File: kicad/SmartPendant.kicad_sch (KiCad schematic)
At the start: 51 parts, among them J1 UART, J2 ST-LINK, J3 Conn_01x05, J4 TYPE-C16PIN, J5 Display, Q1 MMBT3904, U1 WEACT BLACKPILL F4X1, U2 AMS1117-3.3, U3 MB85RC256VPNF

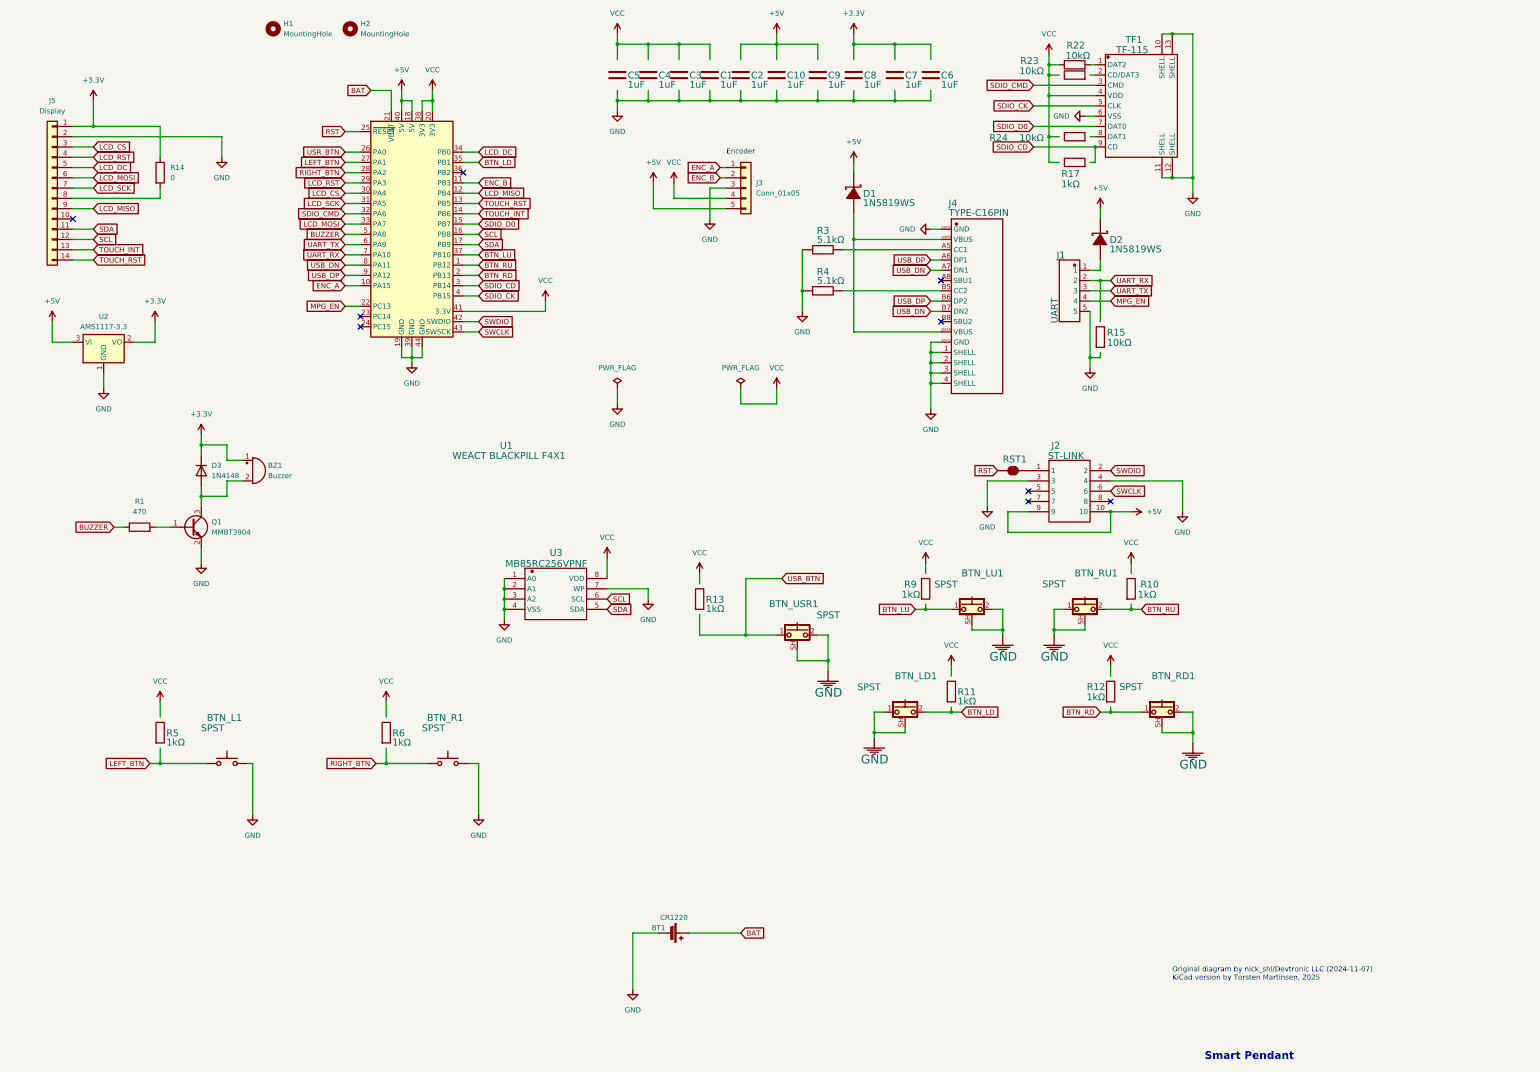
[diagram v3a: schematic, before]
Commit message: Fix ERC violations.
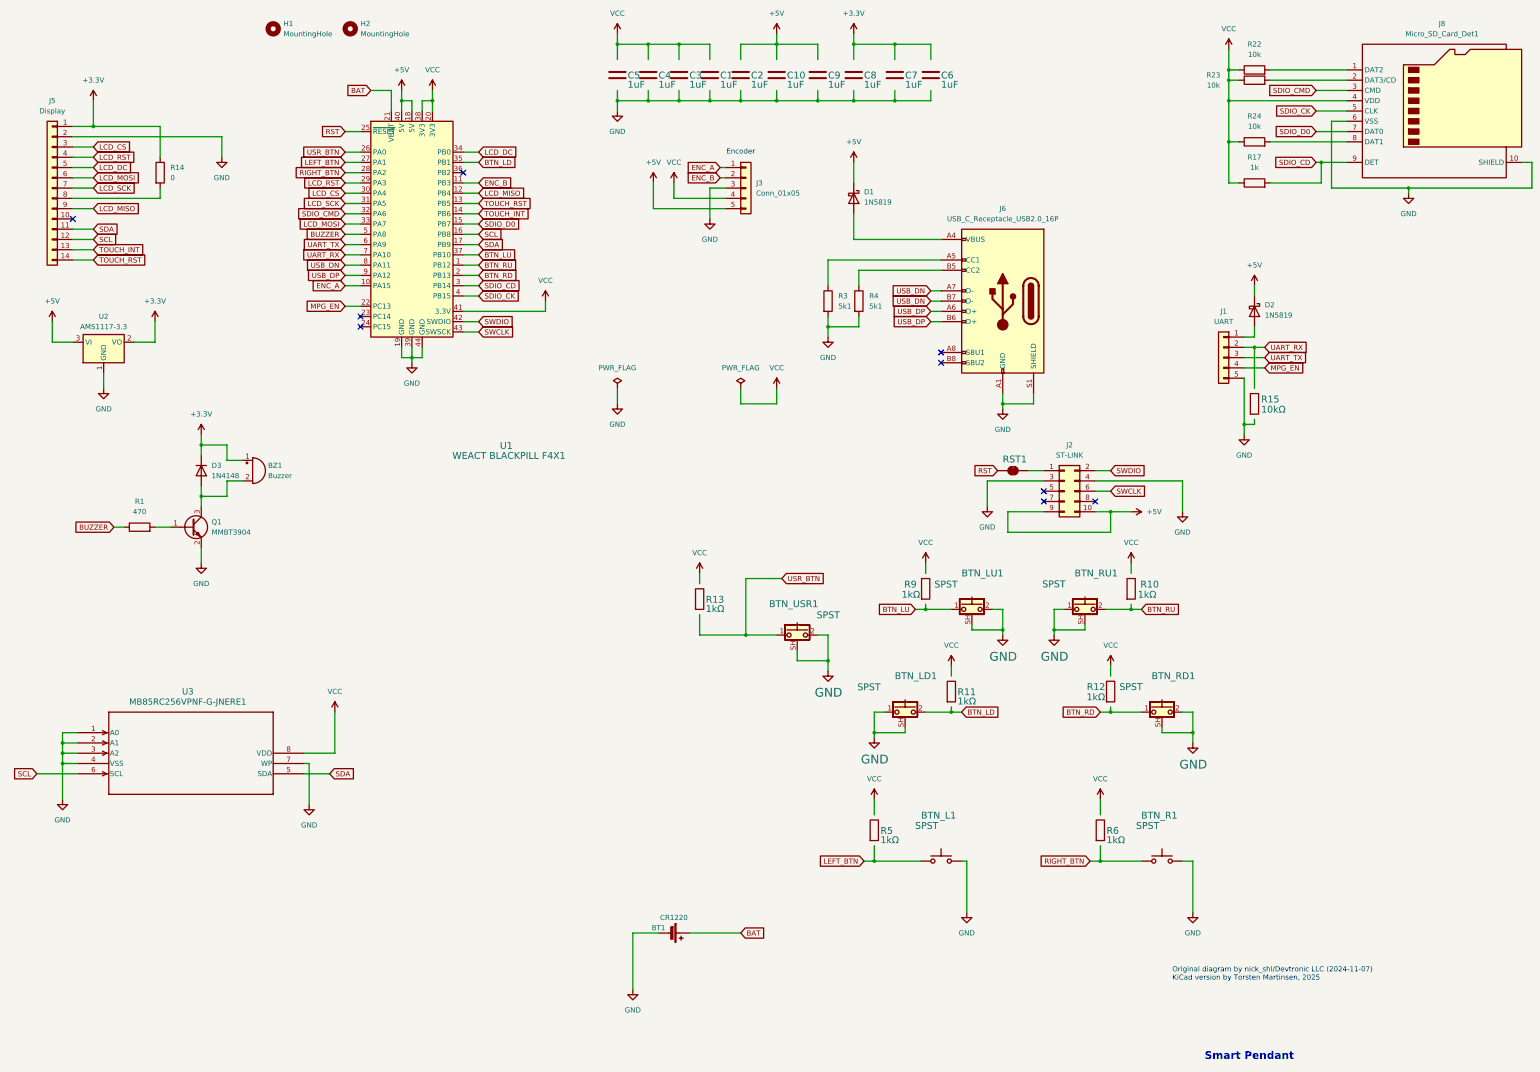
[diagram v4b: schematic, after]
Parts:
- removed D1: 1N5819WS, PCM_Diode_SMD_AKL:D_MiniMELF, symbol B5819WS_C22624
- removed D2: 1N5819WS, PCM_Diode_SMD_AKL:D_MiniMELF, symbol B5819WS_C22624_1
- removed J1: UART, Connector_JST:JST_XH_B5B-XH-A_1x05_P2.50mm_Vertical, symbol KF128-2.54-5P
- removed J2: ST-LINK, Connector_IDC:IDC-Header_2x05_P2.54mm_Horizontal, symbol 300R-10P
- removed J4: TYPE-C16PIN, Custom:USB_C_Receptacle_AliExpress_16pin, symbol TYPE-C16PIN
- removed R17: 1kΩ, PCM_Resistor_SMD_AKL:R_0603_1608Metric, symbol Device:R
- removed R23, R24: 10kΩ, PCM_Resistor_SMD_AKL:R_0603_1608Metric, symbol Device:R
- removed R3: 5.1kΩ, PCM_Resistor_SMD_AKL:R_0603_1608Metric, symbol 0805W8F1002T5E_8
- removed R4: 5.1kΩ, PCM_Resistor_SMD_AKL:R_0603_1608Metric, symbol 0805W8F1002T5E_9
- removed TF1: TF-115, Custom:J_SD_Card-micro_socket_A, symbol TF-115
- removed U3: MB85RC256VPNF, PCM_Package_SO_AKL:SOP-8_3.9x4.9mm_P1.27mm, symbol MB85RC256VPNF
- added D1, D2: 1N5819, PCM_Diode_SMD_AKL:D_SOD-123, symbol Device:D_Schottky
- added J1: UART, Connector_JST:JST_XH_B5B-XH-A_1x05_P2.50mm_Vertical, symbol Connector_Generic:Conn_01x05
- added J2: ST-LINK, Connector_IDC:IDC-Header_2x05_P2.54mm_Horizontal, symbol Connector_Generic:Conn_02x05_Odd_Even
- added J6: USB_C_Receptacle_USB2.0_16P, Custom:USB_C_Receptacle_AliExpress_16pin, symbol Connector:USB_C_Receptacle_USB2.0_16P
- added J8: Micro_SD_Card_Det1, Custom:J_SD_Card-micro_socket_A, symbol Connector:Micro_SD_Card_Det1
- added R17: 1k, PCM_Resistor_SMD_AKL:R_0603_1608Metric, symbol Device:R
- added R23, R24: 10k, PCM_Resistor_SMD_AKL:R_0603_1608Metric, symbol Device:R
- added R3, R4: 5k1, PCM_Resistor_SMD_AKL:R_0603_1608Metric, symbol Device:R
- added U3: MB85RC256VPNF-G-JNERE1, FPT-8P-M02_FUJ, symbol MB85RC256VPNF:MB85RC256VPNF-G-JNERE1
- R22: value 10kΩ -> 10k; Manufacturer UNI-ROYAL(厚声) -> (none); Manufacturer Part 0805W8F1002T5E -> (none); Supplier LCSC -> (none); Supplier Part C17414 -> (none)
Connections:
- net +5V: now also D1.1 (K), D2.1 (K), J2.10 (Pin_10), J2.9 (Pin_9)
- net GND: now also J1.5 (Pin_5), J2.3 (Pin_3), J2.4 (Pin_4), J6.A1 (GND), J6.A12 (GND), J6.B1 (GND), J6.B12 (GND), J6.S1 (SHIELD), J8.10 (SHIELD), J8.6 (VSS), R3.2, R4.2, U3.1 (A0), U3.2 (A1), U3.3 (A2), U3.4 (VSS), U3.7 (WP); no longer BTN_LD1.1, BTN_LD1.SH (B), BTN_LU1.2, BTN_LU1.SH (B), BTN_RD1.2, BTN_RD1.SH (B), BTN_RU1.1, BTN_RU1.SH (B), BTN_USR1.2, BTN_USR1.SH (B)
- net MPG_EN: now also J1.4 (Pin_4)
- net SCL: now also U3.6 (SCL)
- net SDA: now also U3.5 (SDA)
- net SDIO_CD: now also J8.9 (DET), R17.2
- net SDIO_CK: now also J8.5 (CLK)
- net SDIO_CMD: now also J8.3 (CMD)
- net SDIO_D0: now also J8.7 (DAT0)
- net SWCLK: now also J2.6 (Pin_6)
- net SWDIO: now also J2.2 (Pin_2)
- net UART_RX: now also J1.2 (Pin_2)
- net UART_TX: now also J1.3 (Pin_3)
- net USB_DN: now also J6.A7 (D-), J6.B7 (D-)
- net USB_DP: now also J6.A6 (D+), J6.B6 (D+)
- net VCC: now also J8.4 (VDD), R17.1, R23.1, R24.1, U3.8 (VDD)
- net at RST1.2 (B): now also J2.1 (Pin_1)
- net at R22.2: now also J8.1 (DAT2)
- new net: D2.2 (A), J1.1 (Pin_1)
- new net: BTN_LU1.2, BTN_LU1.SH (B)
- new net: D1.2 (A), J6.A4 (VBUS), J6.A9 (VBUS), J6.B4 (VBUS), J6.B9 (VBUS)
- new net: BTN_USR1.2, BTN_USR1.SH (B)
- new net: J6.A5 (CC1), R3.1
- new net: J6.B5 (CC2), R4.1
- new net: BTN_RU1.1, BTN_RU1.SH (B)
- new net: J8.2 (DAT3/CD), R23.2
- new net: BTN_RD1.2, BTN_RD1.SH (B)
- new net: J8.8 (DAT1), R24.2
- new net: BTN_LD1.1, BTN_LD1.SH (B)
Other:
- moved on the sheet: BTN_L1, BTN_R1, R15, R5, R6

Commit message: Use angle JST connectors.
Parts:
- J1: footprint Connector_JST:JST_XH_B5B-XH-A_1x05_P2.50mm_Vertical -> Custom:JST_XH_S5B-XH-A_1x05_P2.50mm_Horizontal_Compact
- J3: value Conn_01x05 -> Encoder; footprint Connector_JST:JST_XH_B5B-XH-A_1x05_P2.50mm_Vertical -> Custom:JST_XH_S5B-XH-A_1x05_P2.50mm_Horizontal_Compact
- U3: footprint FPT-8P-M02_FUJ -> PCM_Package_SO_AKL:SOP-8_3.9x4.9mm_P1.27mm
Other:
- note removed: "Encoder"
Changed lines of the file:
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@@
 		)
 	)
-	(text "Encoder"
-		(exclude_from_sim no)
-		(at 195.58 53.34 0)
-		(effects
-			(font
-				(size 1.27 1.27)
-			)
-		)
-	)
 	(junction
 		(at 260.35 171.45)
@@
 			)
 		)
-		(property "Footprint" "FPT-8P-M02_FUJ"
+		(property "Footprint" "PCM_Package_SO_AKL:SOP-8_3.9x4.9mm_P1.27mm"
 			(at 31.75 196.85 0)
 			(effects
@@
 			)
 		)
-		(property "Footprint" "Connector_JST:JST_XH_B5B-XH-A_1x05_P2.50mm_Vertical"
+		(property "Footprint" "Custom:JST_XH_S5B-XH-A_1x05_P2.50mm_Horizontal_Compact"
 			(at 314.96 104.14 0)
 			(effects
@@
 			)
 		)
-		(property "Value" "Conn_01x05"
+		(property "Value" "Encoder"
 			(at 199.39 63.4999 0)
 			(effects
@@
 			)
 		)
-		(property "Footprint" "Connector_JST:JST_XH_B5B-XH-A_1x05_P2.50mm_Vertical"
+		(property "Footprint" "Custom:JST_XH_S5B-XH-A_1x05_P2.50mm_Horizontal_Compact"
 			(at 196.85 62.23 0)
 			(effects

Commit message: Set provisional footprint for buzzer.
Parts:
- BZ1: footprint (none) -> Buzzer_Beeper:MagneticBuzzer_PUI_AT-0927-TT-6-R
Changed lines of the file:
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@@
 			)
 		)
-		(property "Footprint" ""
+		(property "Footprint" "Buzzer_Beeper:MagneticBuzzer_PUI_AT-0927-TT-6-R"
 			(at 74.295 129.54 90)
 			(effects

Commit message: Change front buttons.
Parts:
- BTN_L1, BTN_R1: footprint Button_Switch_SMD:SW_Push_1P1T_XKB_TS-1187A -> Button_Switch_SMD:SW_SPST_CK_RS282G05A3
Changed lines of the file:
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@@
 			)
 		)
-		(property "Footprint" "Button_Switch_SMD:SW_Push_1P1T_XKB_TS-1187A"
+		(property "Footprint" "Button_Switch_SMD:SW_SPST_CK_RS282G05A3"
 			(at 245.11 223.52 0)
 			(effects
@@
 			)
 		)
-		(property "Footprint" "Button_Switch_SMD:SW_Push_1P1T_XKB_TS-1187A"
+		(property "Footprint" "Button_Switch_SMD:SW_SPST_CK_RS282G05A3"
 			(at 299.72 223.52 0)
 			(effects

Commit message: Correct last footprints.
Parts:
- BZ1: footprint Buzzer_Beeper:MagneticBuzzer_PUI_AT-0927-TT-6-R -> Custom:Buzzer_4.7x9.4mm
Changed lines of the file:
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@@
 			)
 		)
-		(property "Footprint" "Buzzer_Beeper:MagneticBuzzer_PUI_AT-0927-TT-6-R"
+		(property "Footprint" "Custom:Buzzer_4.7x9.4mm"
 			(at 74.295 129.54 90)
 			(effects
